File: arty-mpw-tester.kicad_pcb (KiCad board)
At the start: 4 copper layers, 53.3 x 61.5 mm, 177 parts, among them J1 USB4105-GF-A, J10 61300211121, J11 61300211121, J12 61300211121, J14 61300311121, J15 61300311121, J18 61300411121, J19 61300711121, J20 61300411121, J3 arty_chipKIT_connector, J4 61300211121, J5 61300311121, J6 61300211121, J7 61300211121, J8 61300211121, J9 61300211121, Q1 DTC014TEBTL, SW1 JS202011JCQN, SW3 JS202011JCQN, U1 PAC1954T-E/4MX, U10 TPD4E02B04DQA, U11 TAR5S33UTE85LF, U2 FT4232H-56Q, U3 PAC1954T-E/4MX, U4 MAX811REUS+T, U5 NTS0102DP, U6 MCP4661-103E/ML, U7 Caravel_breakout_PCB_flexypin, U8 W25Q32FVSS, U9 MIC2211-AAYML-TR, Y1 ABM8G-12.000MHZ-18-D2Y-T, Y2 ECS-2520MVLC-100-BN-TR

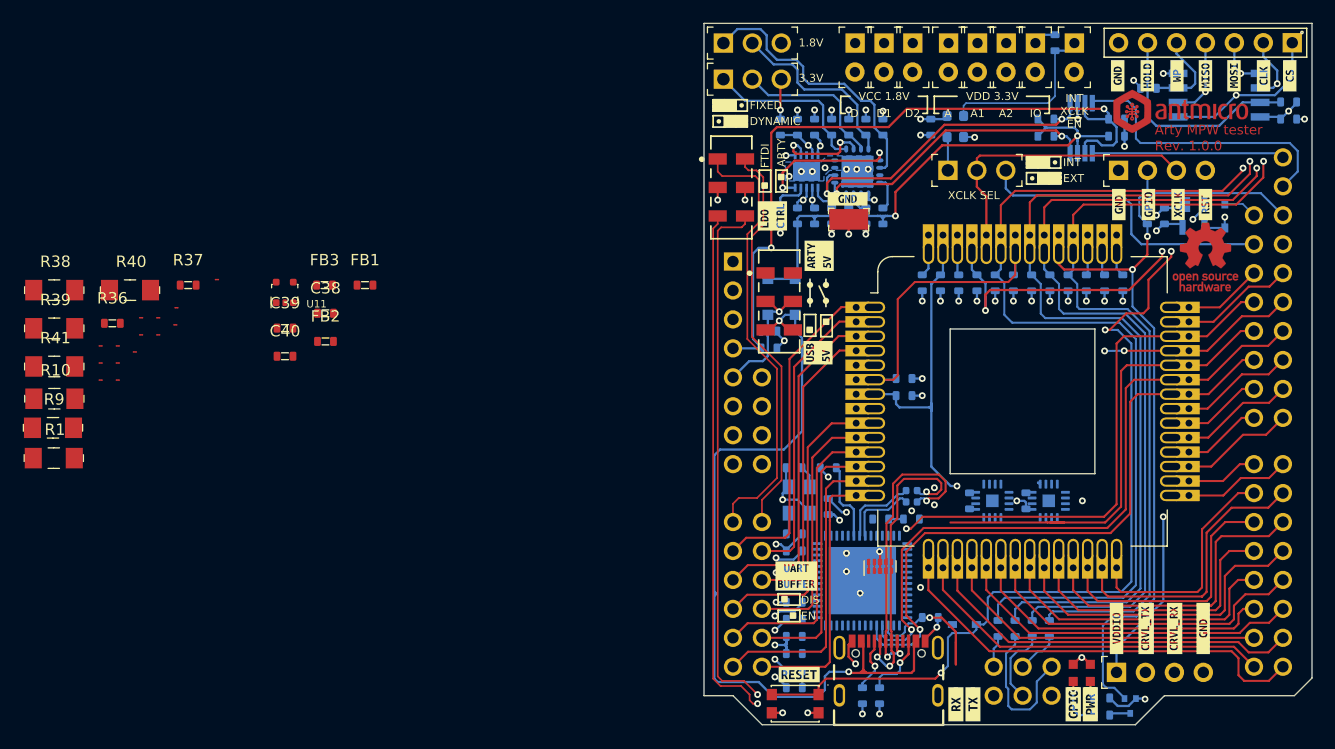
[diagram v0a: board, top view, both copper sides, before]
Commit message: Moved and reconnected power supply unit. Placed shunt resistors
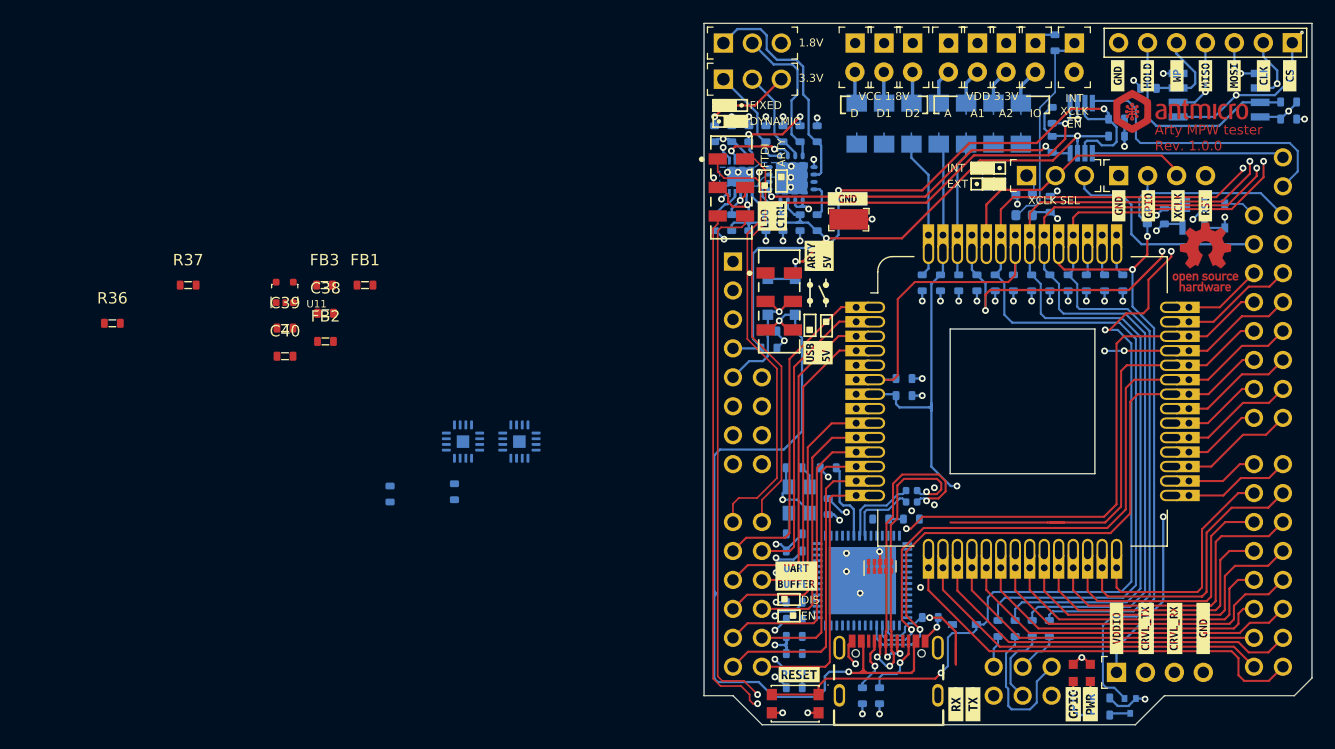
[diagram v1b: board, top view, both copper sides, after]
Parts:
- NT1, NT10, NT11, NT12, NT13, NT14, NT2, NT3, NT4, NT5, NT6, NT7, NT8, NT9, R1, R10, R38, R39, R40, R41, R9: moved to B.Cu
- moved R38 86.1 mm to (150.8, 74.8), turned to -90 degrees
- moved R39 84.4 mm to (148.4, 74.8), turned to -90 degrees
- moved R1 83.0 mm to (143.6, 74.8), turned to -90 degrees
- moved NT9 82.8 mm to (150.8, 75.8), turned to -90 degrees
- moved NT2 82.2 mm to (150.8, 73.8), turned to 90 degrees
- moved NT10 80.9 mm to (148.4, 75.8), turned to -90 degrees
- moved R10 79.0 mm to (141.2, 74.8), turned to -90 degrees
- moved NT11 78.9 mm to (146.0, 75.8), turned to -90 degrees
- moved R9 77.7 mm to (138.8, 74.8), turned to -90 degrees
- moved NT4 75.9 mm to (146.0, 73.8), turned to 90 degrees
- moved R40 74.8 mm to (146.0, 74.8), turned to -90 degrees
- moved NT3 74.2 mm to (148.4, 73.8), turned to 90 degrees
- moved R41 73.6 mm to (136.4, 74.8), turned to -90 degrees
- moved NT13 70.6 mm to (138.8, 75.8), turned to -90 degrees
- moved NT7 70.3 mm to (141.2, 73.8), turned to 90 degrees
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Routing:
- net /VCCD2: track 3.72 -> 12.3 mm
- net /VDDA2: track 3.38 -> 11.7 mm
- net /VDDIO: track 66.4 -> 74.5 mm
- net /ARTY_XCLK: track 26.9 -> 19.6 mm
- net /ARTY_SDA: track 28.7 -> 35.3 mm
- net +3V3: track 19.1 -> 25.1 mm, vias 13 -> 12
- net /P1B: track 14.9 -> 9.30 mm
- net /P1A: track 13.3 -> 8.19 mm
- net /EN_VOUT2: track 8.48 -> 3.55 mm, vias 2 -> 1
- net /EN_VOUT1: track 11.5 -> 6.59 mm
- net /LV_BOOSTER: track 3.42 -> 7.90 mm
- net /P0B: track 24.3 -> 20.2 mm
- net /5V0: track 57.7 -> 61.7 mm, vias 2 -> 3
- net /3V3_ARTY: track 63.6 -> 60.0 mm
- net /CRVL_XCLK: track 26.8 -> 23.2 mm
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
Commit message: Finished initial routing. Corrected switch footprint
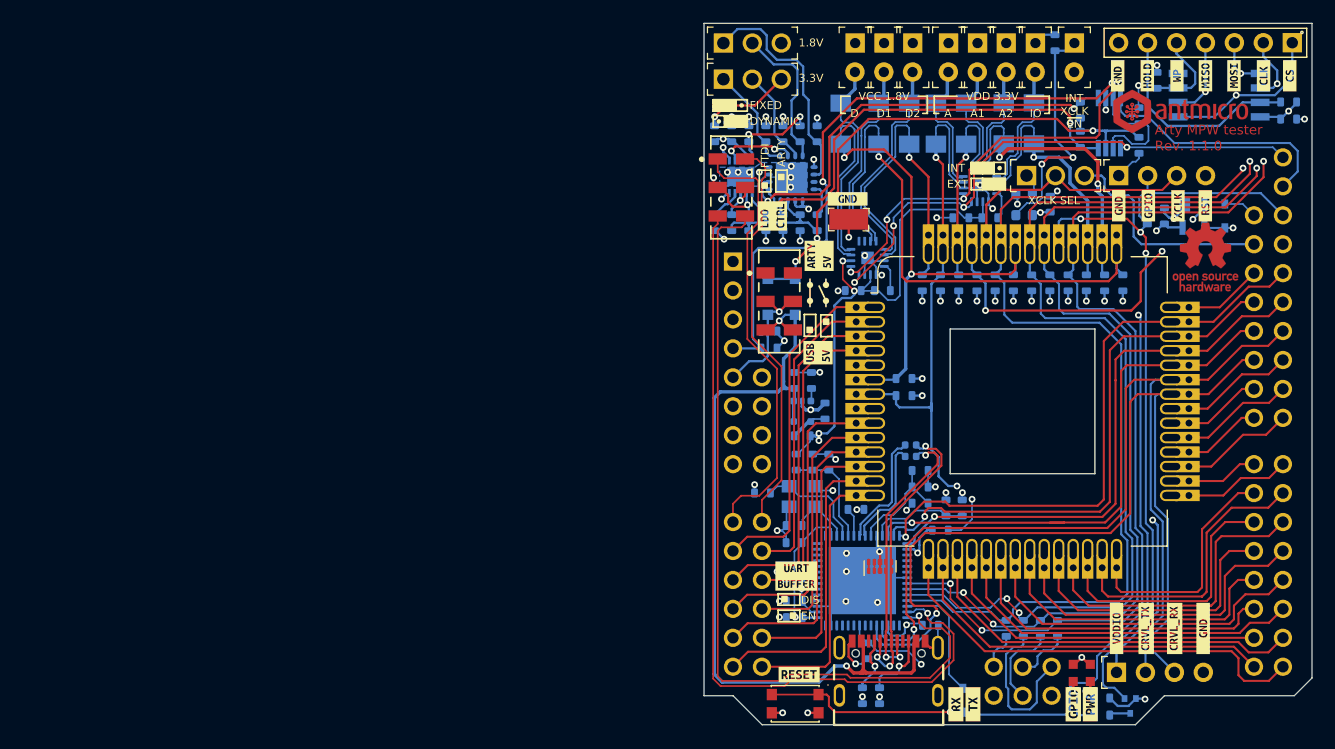
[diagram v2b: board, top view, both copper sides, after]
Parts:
- C38, C39, C40, FB1, FB2, FB3, R36, R37, U11: moved to B.Cu
- C7: value C_4u7_0603 -> C_100n_0603
- NT1, NT10, NT11, NT12, NT13, NT14, NT2, NT3, NT4, NT5, NT6, NT7, NT8, NT9: footprint antmicro-footprints:NetTie-2_SMD_Pad0.127mm -> antmicro-footprints:NetTie-2_SMD_Pad0.15mm
- moved R36 77.5 mm to (148.1, 83.1)
- moved R37 60.9 mm to (138.7, 89.5)
- moved C39 58.5 mm to (137.4, 121.1), turned to -90 degrees
- moved C38 57.2 mm to (143.7, 110.5)
- moved FB2 54.1 mm to (142.0, 108.1)
- moved C40 48.7 mm to (130.9, 114.7), turned to 180 degrees
- moved U11 46.6 mm to (131.6, 100.0)
- moved U1 46.3 mm to (147.2, 80.2), turned to 90 degrees
- moved FB3 44.0 mm to (131.6, 102.2)
- moved FB1 40.9 mm to (131.1, 104.5), turned to -90 degrees
- moved C10 40.9 mm to (142.0, 106.7), turned to 0 degrees
- moved U3 39.0 mm to (137.3, 86.6), turned to 90 degrees
- moved C18 35.7 mm to (130.9, 111.6), turned to 180 degrees
- moved C2 34.0 mm to (145.5, 83.1)
- moved C4 23.4 mm to (136.1, 89.5)
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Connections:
- U1 pad 10: /VDDA2_SEN+ -> /VDDA2_SEN_+
- U1 pad 11: /VDDIO_SEN+ -> /VDDA1_SEN_+
- U1 pad 12: /VDDIO_SEN- -> /VDDA1_SEN_-
- U1 pad 13: /VDDA_SEN+ -> /VDDA_SEN_+
- U1 pad 14: /VDDA_SEN- -> /VDDA_SEN_-
- U1 pad 7: /VDDA1_SEN- -> /VDDIO_SEN_-
- U1 pad 8: /VDDA1_SEN+ -> /VDDIO_SEN_+
- U1 pad 9: /VDDA2_SEN- -> /VDDA2_SEN_-
- U3 pad 11: /VCCD_SEN+ -> /VCCD1_SEN_+
- U3 pad 12: /VCCD_SEN- -> /VCCD1_SEN_-
- U3 pad 13: /VCCD1_SEN+ -> /VCCD2_SEN_+
- U3 pad 14: /VCCD1_SEN- -> /VCCD2_SEN_-
- U3 pad 7: /VCCD2_SEN- -> /VCCD_SEN_-
- U3 pad 8: /VCCD2_SEN+ -> /VCCD_SEN_+
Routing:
- net 3V3_FTDI: track 4.02 -> 63.0 mm, vias 2 -> 9
- net CRVL_IO1: track 11.6 -> 52.7 mm, vias 0 -> 1
- net EP: track 71.9 -> 106.0 mm, vias 58 -> 65
- net /ARTY_SDA_3V3: track 25.1 -> 58.7 mm, vias 1 -> 4
- net /VCCD1: track 3.72 -> 37.3 mm, vias 2 -> 1
- net /ARTY_SCL_3V3: track 16.4 -> 48.9 mm, vias 0 -> 4
- net CRVL_IO3: track 17.4 -> 49.5 mm, vias 2 -> 1
- net CRVL_IO5: track 59.2 -> 87.5 mm
- net FTDI_EN_VOUT1: track 45.9 -> 70.9 mm
- net FTDI_EN_VOUT2: track 46.6 -> 70.9 mm
- net /VDDA1: track 3.58 -> 20.9 mm, vias 0 -> 2
- net /VCCD2_SEN_+: track 0.00 -> 16.0 mm
- net /VCCD2_SEN_-: track 0.00 -> 16.0 mm
- net /VCCD: track 28.8 -> 43.8 mm, vias 0 -> 2
- net /VCCD_SEN_+: track 0.00 -> 14.3 mm
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- added copper zone on In2.Cu, net 3V3_FTDI
- removed copper zone on In2.Cu, net /ARTY_SDA_3V3
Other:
- board text added: "Rev. 1.1.0"
- board text removed: "Rev. 1.0.0"

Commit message: Cleared DRC. Updated stackup. Optimized paths
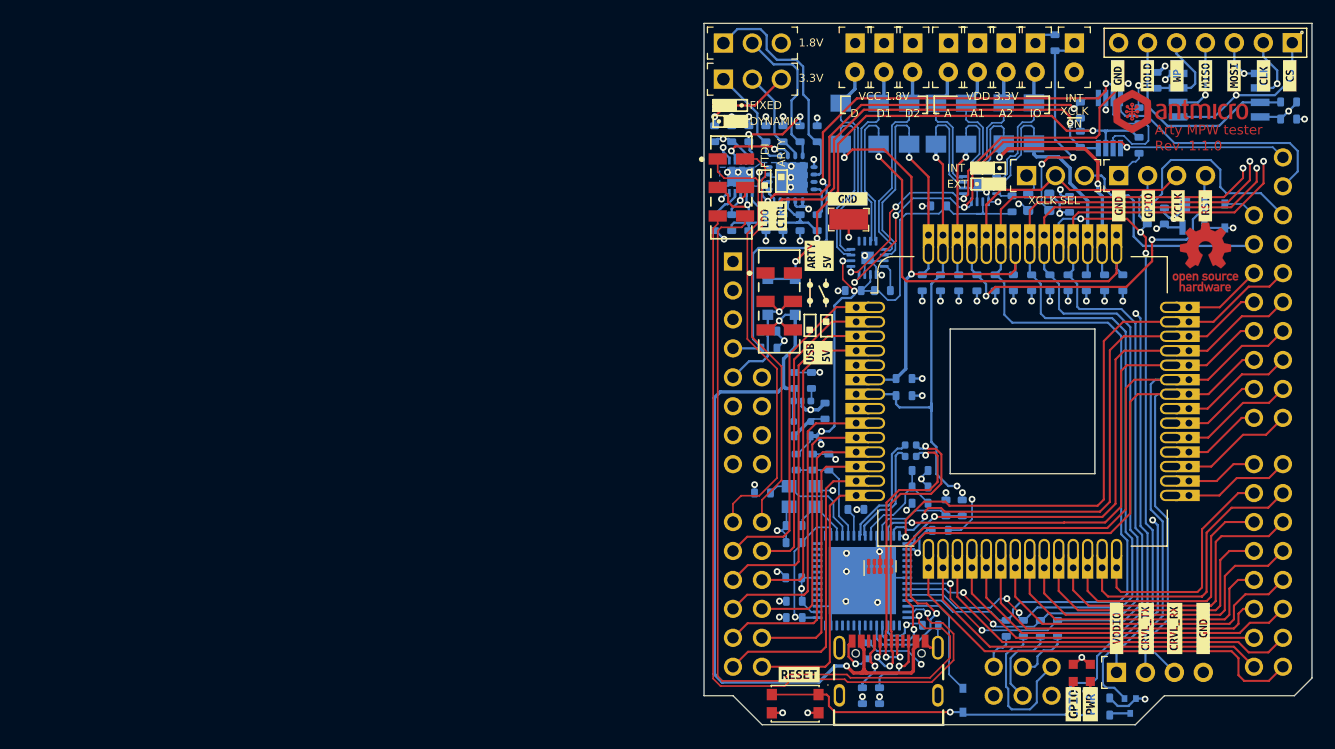
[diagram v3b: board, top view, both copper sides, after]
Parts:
- removed kibuzzard-638F9F3B: G***, kibuzzard-638F9F3B
- removed kibuzzard-638F9F40: G***, kibuzzard-638F9F40
- removed kibuzzard-63938B4C: G***, kibuzzard-63938B4C
- moved R36 2.30 mm to (150.0, 81.8), turned to 90 degrees
- moved C2 2.20 mm to (143.6, 82.0)
- moved C19 1.70 mm to (155.1, 81.9)
- moved Y2 1.30 mm to (152.4, 81.7), turned to 90 degrees
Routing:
- net EP: track 106.0 -> 94.6 mm
- net Net-(J3-Pad49): track 13.7 -> 17.8 mm
- net /CRVL_~{RST}: track 36.3 -> 32.5 mm, vias 3 -> 2
- net 3V3_FTDI: track 63.0 -> 65.4 mm
- net /FTDI/USB_DN: track 26.4 -> 28.0 mm
- net /FTDI/USB_DP: track 24.7 -> 26.2 mm
- net /XCLK_EN: track 19.9 -> 18.4 mm
- net /ARTY_SDA_3V3: track 58.7 -> 60.1 mm
- net Net-(R36-Pad2): track 2.55 -> 1.24 mm
- net /VCCD2_SEN_-: track 16.0 -> 14.7 mm
- net /VCCD2_SEN_+: track 16.0 -> 14.7 mm
- net CRVL_IO4: track 48.2 -> 47.0 mm
- net /EN_VOUT1: track 6.59 -> 5.35 mm, vias 2 -> 1
- net +3V3: track 24.3 -> 25.3 mm
- net /VCCD1_SEN_+: track 13.5 -> 12.6 mm
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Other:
- board text added: "Arty MPW tester Rev. 1.1.0 12/2022"
- board text removed: "Arty MPW tester Rev. 1.0.0 12/2022"
- board text removed: "DIS"
- board text removed: "EN"

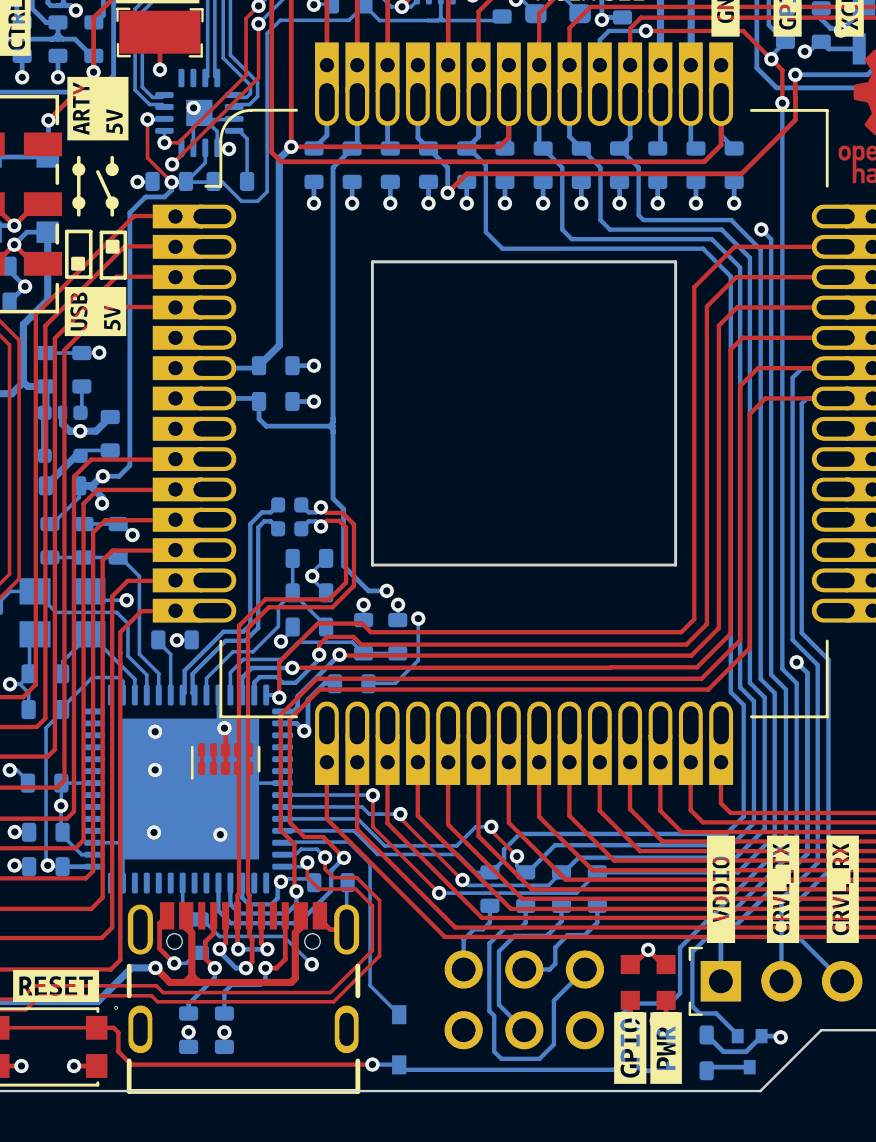
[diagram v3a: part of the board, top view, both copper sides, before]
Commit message: Optimized some paths. orrected power plane under USB tracks
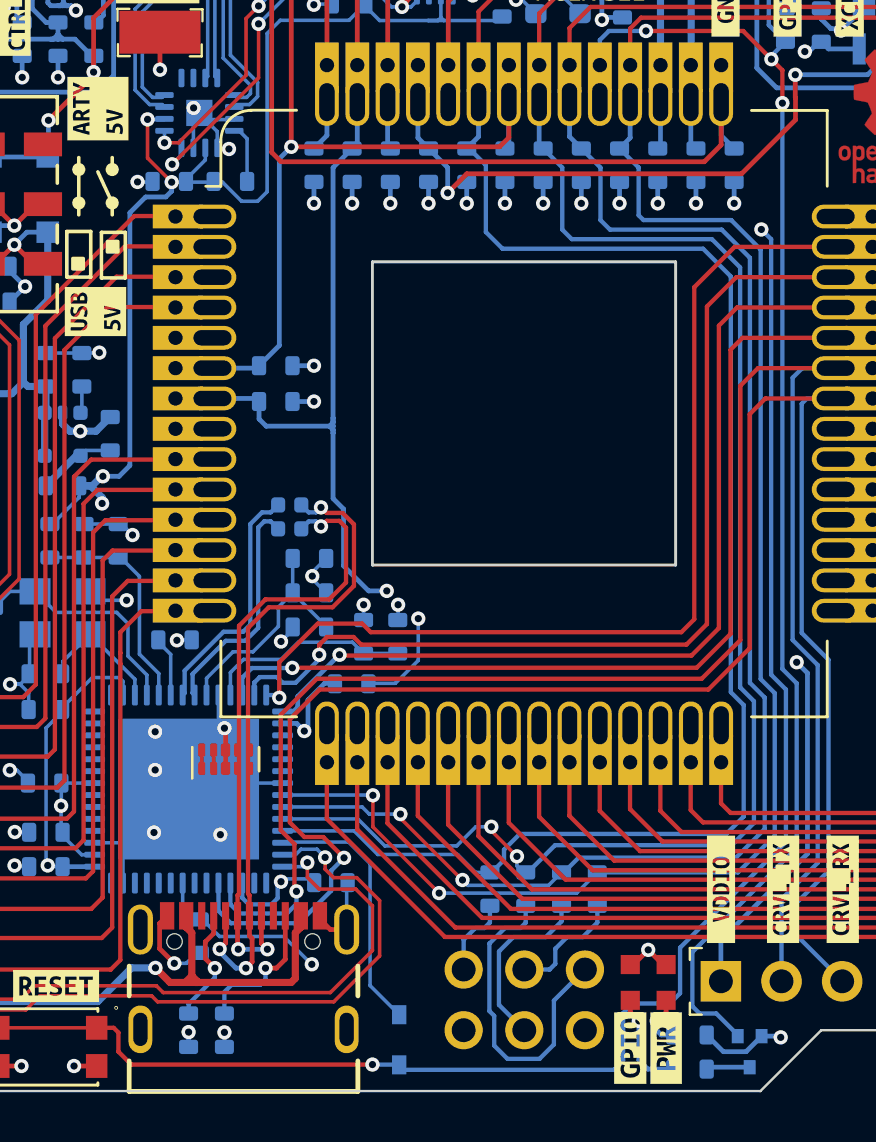
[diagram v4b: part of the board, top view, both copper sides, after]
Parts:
- moved R12 0.07 mm to (157.9, 126.6)
